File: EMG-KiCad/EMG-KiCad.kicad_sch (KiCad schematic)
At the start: 30 parts, among them J1 Conn_01x03_Socket, J2 Conn_01x03_Socket, U1 AD623, U2 OPA1662D, U3 OPA1662D, U4 OPA1662D, U5 OPA1662D, U6 OPA1662D, U7 LDO 3.3, U8 LDO 1.5

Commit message: Full circuit
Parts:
- added C11, C12, C13, C14, C15, C16, C17, C18: C_Small, symbol Device:C_Small
- added R9: R_Small, symbol Device:R_Small
- added unit 1 of U5
- added U9: OPA1662D, Package_SO:SOIC-8_3.9x4.9mm_P1.27mm, symbol Amplifier_Operational:OPA1662D
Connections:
- net Earth: now also J2.3 (Pin_3), C11.2, C12.2, C13.2, C14.2, C15.2, C16.1, C17.2, C18.2
- net V+: now also C10.1, C9.1, U7.5 (OUT), U8.1 (IN), C12.1, C13.1, C16.2, U9.8 (V+)
- net V-: now also U9.4 (V-)
- net Vref: now also C17.1, C18.1, R9.1
- net Vout: now reaches C4.2, J2.1 (Pin_1), R10.2, U3.7
- net Vpower: now reaches C8.1, J2.2 (Pin_2), U7.1 (IN)
- net Vpower: now also C11.1
- net at U8.5 (OUT): now also C14.1, C15.1, U5.3 (+)
- new net: R9.2, U5.1, U5.2 (-)
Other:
- moved on the sheet: C10, C8, C9

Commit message: Complete schematic and add custom library
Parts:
- removed C6: C_Small, symbol Device:C_Small
- removed J2: Conn_01x03_Socket, symbol Connector:Conn_01x03_Socket
- removed U2, U3, U4, U5, U6, U9: OPA1662D, Package_SO:SOIC-8_3.9x4.9mm_P1.27mm, symbol Amplifier_Operational:OPA1662D
- added C19: C_Small, Capacitor_SMD:C_0603_1608Metric_Pad1.08x0.95mm_HandSolder, symbol Device:C_Small
- added J3: Conn_01x02_Socket, Connector_Samtec_HPM_THT:Samtec_HPM-02-05-x-S_Straight_1x02_Pitch5.08mm, symbol Connector:Conn_01x02_Socket
- added J4: Conn_01x01_Socket, Connector_Samtec_HPM_THT:Samtec_HPM-01-05-x-S_Straight_1x01_Pitch5.08mm, symbol Connector:Conn_01x01_Socket
- added R12, R13: R_Small, Resistor_SMD:R_0603_1608Metric_Pad0.98x0.95mm_HandSolder, symbol Device:R_Small
- added U1, U2: OPA2333xxD, Package_SO:SOIC-8_3.9x4.9mm_P1.27mm, symbol Amplifier_Operational:OPA2333xxD
- added U3: OPA333xxDBV, Package_TO_SOT_SMD:SOT-23-5, symbol Amplifier_Operational:OPA333xxDBV
- added U4: OPA350UA, Package_SO:SOIC-8_5.3x6.2mm_P1.27mm, symbol LIMB_EMG_Library:OPA350UA
- C1, C10, C11, C12, C13, C14, C15, C16, C17, C18, C2, C3, C4, C5, C7, C8, C9: footprint (none) -> Capacitor_SMD:C_0603_1608Metric_Pad1.08x0.95mm_HandSolder
- J1: footprint (none) -> Connector_Samtec_HPM_THT:Samtec_HPM-03-05-x-S_Straight_1x03_Pitch5.08mm
- R1, R10, R11, R2, R3, R4, R5, R6, R7, R8, R9: footprint (none) -> Resistor_SMD:R_0603_1608Metric_Pad0.98x0.95mm_HandSolder
- U0: renamed from U1; footprint (none) -> Package_SO:SOIC-8_5.3x6.2mm_P1.27mm
- renumbered U7 to U5, U8 to U6
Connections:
- net Earth: now also C7.2, C19.1, J3.2 (Pin_2), U1.4 (V-), U2.4 (V-), U3.2 (V-), U4.4 (V-); no longer C7.1
- net V+: now also C7.1, C19.2, U1.8 (V+), U2.8 (V+), U3.5 (V+), U4.8 (V+); no longer C10.1, C13.1, C7.2, U6.1 (IN)
- net Vout: now also J4.1 (Pin_1), U3.1
- net Vpower: now also C10.1, C13.1, U6.1 (IN), J3.1 (Pin_1)
- net Vref: now also U1.3 (+), U2.3 (+), U2.6 (-), U3.3 (+)
- net at C1.1, U0.5 (Ref): now also U2.7
- net at C1.2, R2.1: now also U2.5 (+)
- net at R4.1, R5.1, R6.2: now also U1.1
- net at C2.2, R5.2: now also U1.2 (-), U1.6 (-), U1.7
- net at C14.1, C15.1, U6.5 (OUT): now also U4.3 (+)
- net at R7.2, R8.2: now also U2.2 (-)
- net at R11.2, R8.1: now also U2.1
- net at C4.1, R10.1, R11.1: now also U3.4 (-)
- net at R9.2: now also U4.1, U4.2 (-)
- net at U0.2 (-): now also R12.2; no longer J1.2 (Pin_2)
- net at J1.3 (Pin_3): now also R13.1; no longer U0.3 (+)
- net at R1.2, R3.2: now also U1.5 (+)
- new net: R13.2, U0.3 (+)
- new net: J1.2 (Pin_2), R12.1
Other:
- moved on the sheet: C1, C10, C11, C12, C13, C14, C15, C16, C17, C18, C2, C3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

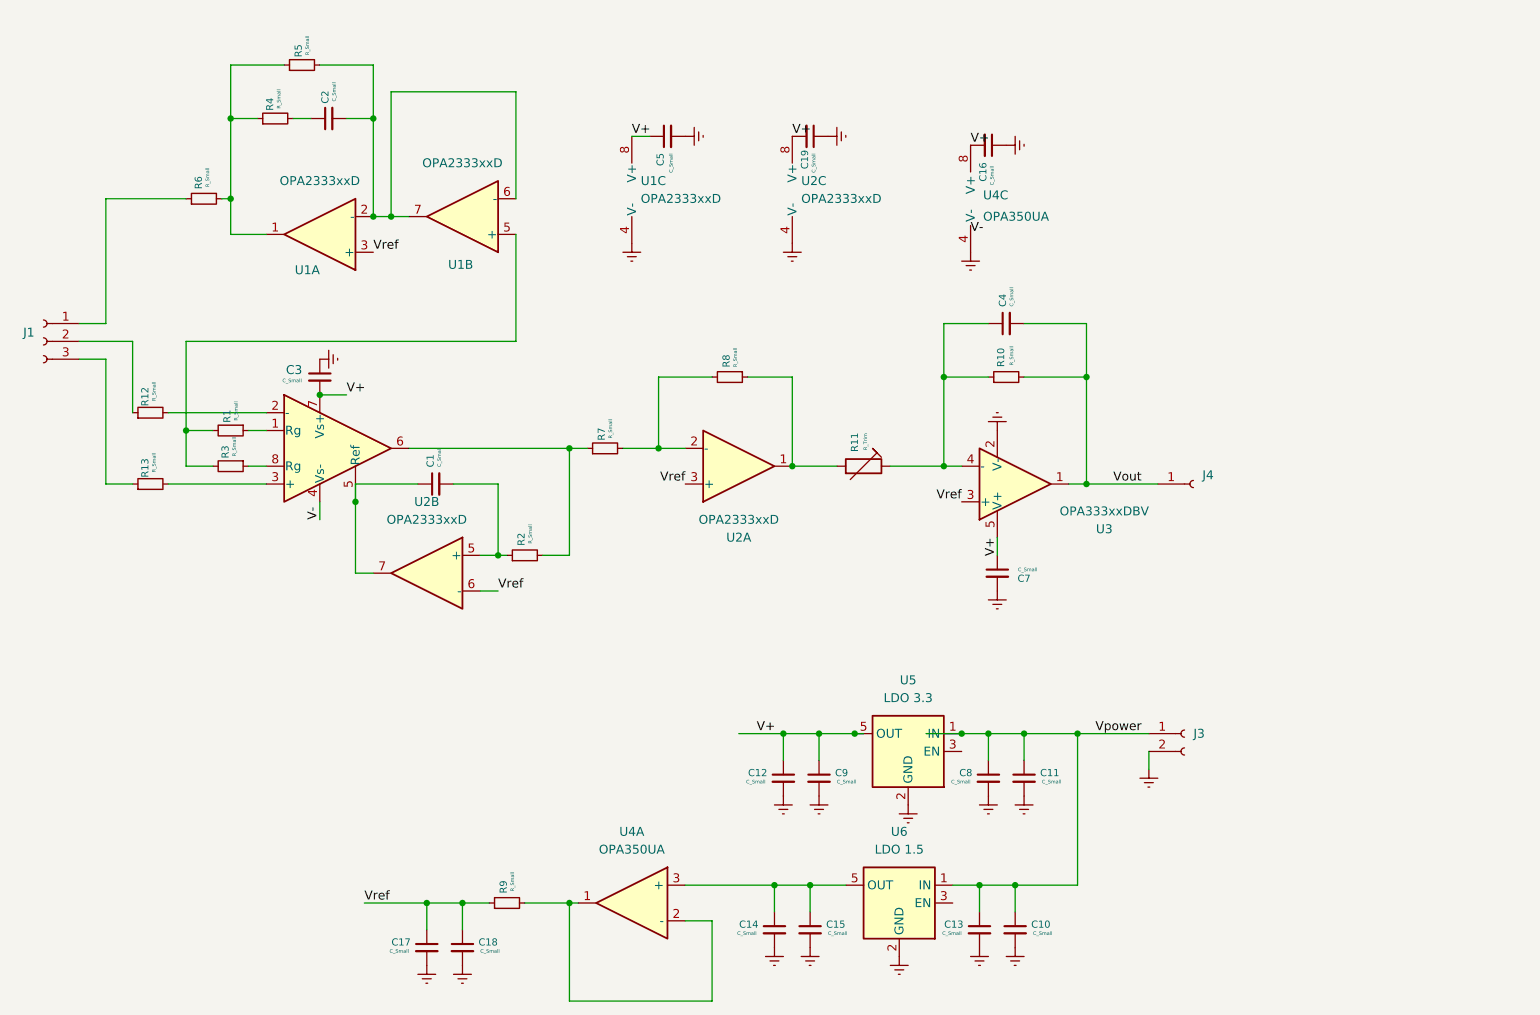
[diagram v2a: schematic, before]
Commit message: add libraries and change schematic
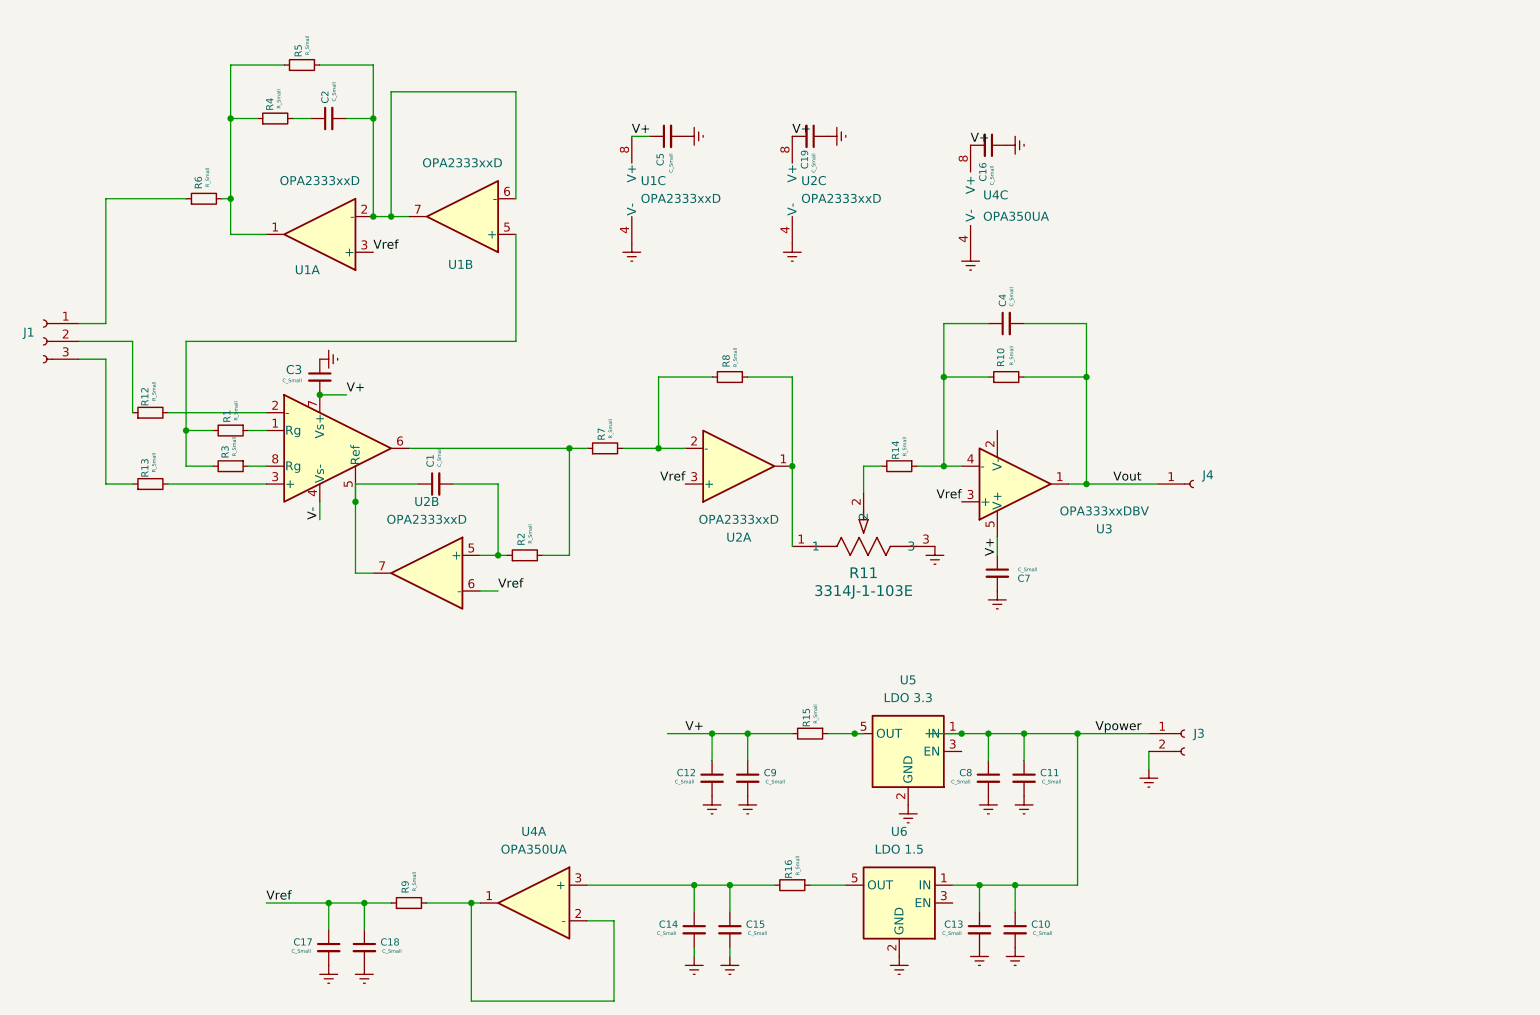
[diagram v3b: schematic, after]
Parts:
- removed R11: R_Trim, Resistor_SMD:R_0603_1608Metric_Pad0.98x0.95mm_HandSolder, symbol Device:R_Trim
- added R11: 3314J-1-103E, POT_3314J, symbol LIMB_EMG:3314J-1-103E
- added R14, R15, R16: R_Small, Resistor_SMD:R_0603_1608Metric_Pad0.98x0.95mm_HandSolder, symbol Device:R_Small
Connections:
- net Earth: now also R11.3; no longer U3.2 (V-)
- net V+: now also R15.2; no longer U5.5 (OUT)
- net at C14.1, C15.1, U4.3 (+): now also R16.2; no longer U6.5 (OUT)
- net at C4.1, R10.1, U3.4 (-): now also R14.1
- net at R8.1, U2.1: now also R11.1
- new net: R16.1, U6.5 (OUT)
- new net: R11.2, R14.2
- new net: R15.1, U5.5 (OUT)
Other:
- moved on the sheet: C12, C14, C15, C17, C18, C9, R9, U4A

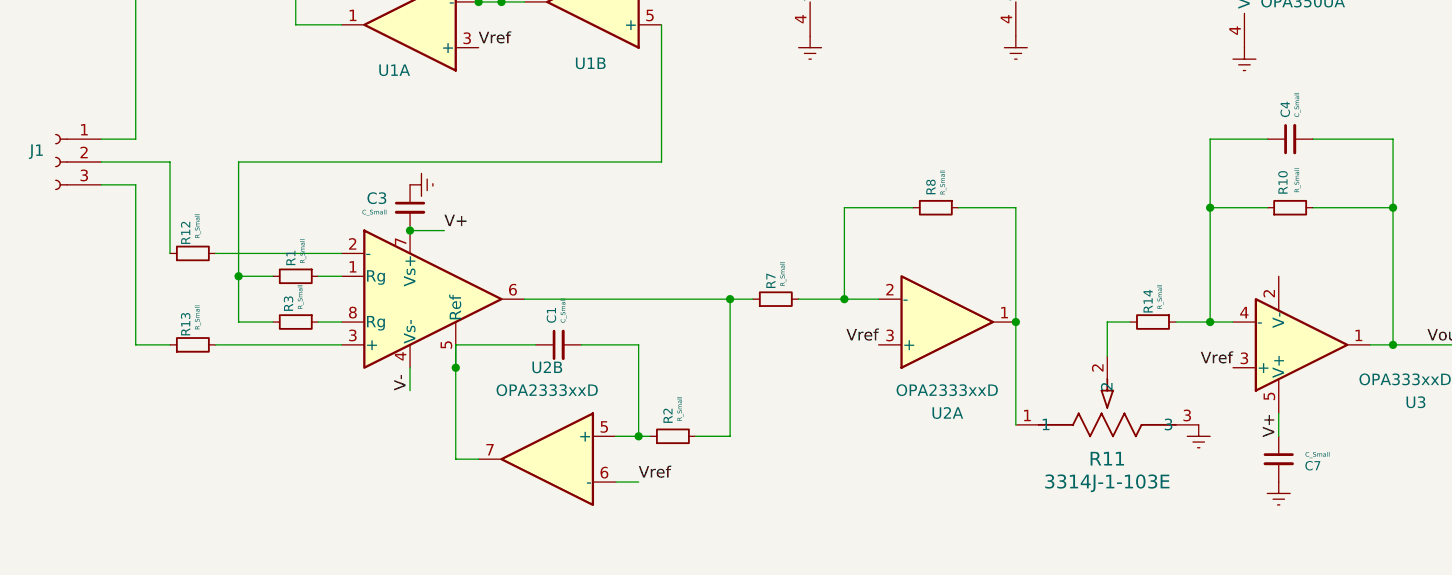
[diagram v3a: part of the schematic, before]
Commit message: complete the pcb traces
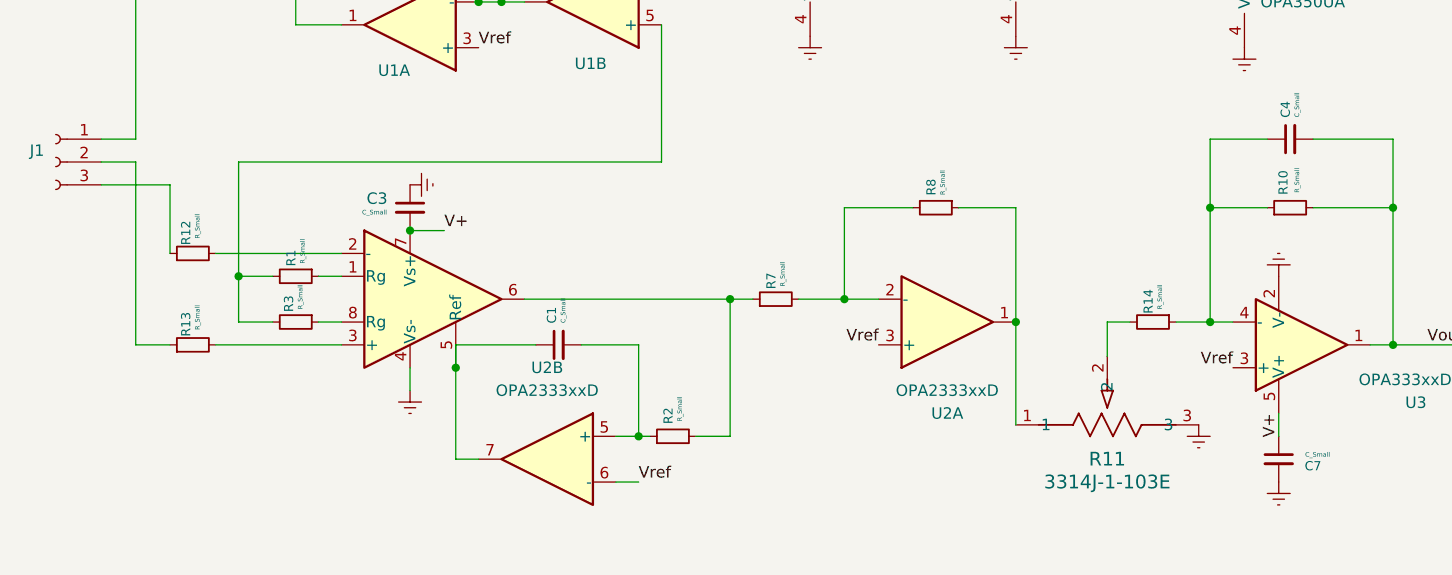
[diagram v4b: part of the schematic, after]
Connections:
- net V- is gone; now on net Earth: U0.4 (Vs-)
- net Earth: now also U3.2 (V-)
- net at R13.1: now also J1.2 (Pin_2); no longer J1.3 (Pin_3)
- net at R12.1: now also J1.3 (Pin_3); no longer J1.2 (Pin_2)
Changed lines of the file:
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@@
 	(wire
 		(pts
-			(xy 69.85 71.12) (xy 69.85 60.96)
-		)
-		(stroke
-			(width 0)
-			(type default)
-		)
-	)
-	(wire
-		(pts
 			(xy 96.52 83.82) (xy 96.52 86.36)
 		)
@@
 	(wire
 		(pts
-			(xy 66.04 63.5) (xy 62.23 63.5)
+			(xy 166.37 138.43) (xy 171.45 138.43)
 		)
 		(stroke
@@
 	(wire
 		(pts
-			(xy 166.37 138.43) (xy 171.45 138.43)
+			(xy 66.04 60.96) (xy 62.23 60.96)
 		)
 		(stroke
@@
 	(wire
 		(pts
-			(xy 69.85 60.96) (xy 62.23 60.96)
-		)
-		(stroke
-			(width 0)
-			(type default)
-		)
-	)
-	(wire
-		(pts
 			(xy 83.82 29.21) (xy 83.82 40.64)
 		)
@@
 	(wire
 		(pts
-			(xy 66.04 81.28) (xy 66.04 63.5)
+			(xy 66.04 60.96) (xy 66.04 81.28)
 		)
 		(stroke
@@
 	(wire
 		(pts
+			(xy 69.85 71.12) (xy 69.85 63.5)
+		)
+		(stroke
+			(width 0)
+			(type default)
+		)
+	)
+	(wire
+		(pts
 			(xy 205.74 66.04) (xy 205.74 81.28)
 		)
@@
 	(wire
 		(pts
+			(xy 69.85 63.5) (xy 62.23 63.5)
+		)
+		(stroke
+			(width 0)
+			(type default)
+		)
+	)
+	(wire
+		(pts
 			(xy 124.46 25.4) (xy 124.46 40.64)
 		)
@@
 		)
 	)
-	(label "V-"
-		(at 96.52 86.36 90)
-		(effects
-			(font
-				(size 1.27 1.27)
-			)
-			(justify left bottom)
-		)
-	)
 	(label "Vref"
 		(at 187.96 83.82 180)
@@
 	)
 	(symbol
+		(lib_id "power:Earth")
+		(at 96.52 86.36 0)
+		(unit 1)
+		(exclude_from_sim no)
+		(in_bom yes)
+		(on_board yes)
+		(dnp no)
+		(fields_autoplaced yes)
+		(property "Reference" "#PWR024"
+			(at 96.52 92.71 0)
+			(effects
+				(font
+					(size 1.27 1.27)
+				)
+				(hide yes)
+			)
+		)
+		(property "Value" "Earth"
+			(at 96.5201 90.17 90)
+			(effects
+				(font
+					(size 1.27 1.27)
+				)
+				(justify right)
+				(hide yes)
+			)
+		)
+		(property "Footprint" ""
+			(at 96.52 86.36 0)
+			(effects
+				(font
+					(size 1.27 1.27)
+				)
+				(hide yes)
+			)
+		)
+		(property "Datasheet" "~"
+			(at 96.52 86.36 0)
+			(effects
+				(font
+					(size 1.27 1.27)
+				)
+				(hide yes)
+			)
+		)
+		(property "Description" "Power symbol creates a global label with name \"Earth\""
+			(at 96.52 86.36 0)
+			(effects
+				(font
+					(size 1.27 1.27)
+				)
+				(hide yes)
+			)
+		)
+		(pin "1"
+		)
+		(instances
+			(project "EMG-KiCad"
+				(path "/f6c8dea7-6a58-4159-9db2-42f13dd699f4"
+					(reference "#PWR024")
+					(unit 1)
+				)
+			)
+		)
+	)
+	(symbol
 		(lib_id "Device:R_Small")
 		(at 93.98 21.59 90)
@@
 					(unit 1)
 				)
+			)
+		)
+	)
+	(symbol
+		(lib_id "power:Earth")
+		(at 193.04 73.66 180)
+		(unit 1)
+		(exclude_from_sim no)
+		(in_bom yes)
+		(on_board yes)
+		(dnp no)
+		(fields_autoplaced yes)
+		(property "Reference" "#PWR023"
+			(at 193.04 67.31 0)
+			(effects
+				(font
+					(size 1.27 1.27)
+				)
+				(hide yes)
+			)
+		)
+		(property "Value" "Earth"
+			(at 193.0399 69.85 90)
+			(effects
+				(font
+					(size 1.27 1.27)
+				)
+				(justify right)
+				(hide yes)
+			)
+		)
+		(property "Footprint" ""
+			(at 193.04 73.66 0)
+			(effects
+				(font
+					(size 1.27 1.27)
+				)
+				(hide yes)
+			)
+		)
+		(property "Datasheet" "~"
+			(at 193.04 73.66 0)
+			(effects
+				(font
+					(size 1.27 1.27)
+				)
+				(hide yes)
+			)
+		)
+		(property "Description" "Power symbol creates a global label with name \"Earth\""
+			(at 193.04 73.66 0)
+			(effects
+				(font
+					(size 1.27 1.27)
+				)
+				(hide yes)
+			)
+		)
+		(pin "1"
+		)
+		(instances
+			(project "EMG-KiCad"
+				(path "/f6c8dea7-6a58-4159-9db2-42f13dd699f4"
+					(reference "#PWR023")
+					(unit 1)
+				)
